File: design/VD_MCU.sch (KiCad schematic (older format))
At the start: 2 parts

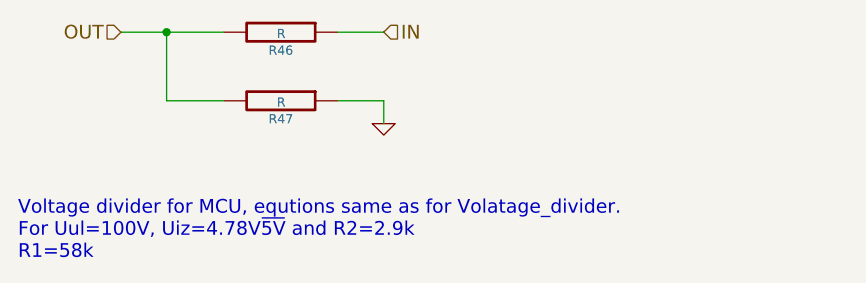
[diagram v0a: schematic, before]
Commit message: Fix some ERC error, add decoupling cap to Vref+ and make some small changes to lib
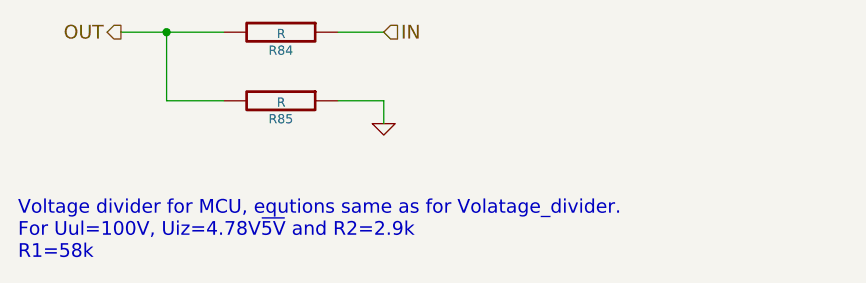
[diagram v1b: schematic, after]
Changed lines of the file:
@@
 AR Path="/54B735D5/54E0E40F/54E0BCE1" Ref="R82"  Part="1"
 AR Path="/54B735D5/54E0E5A3/54E0BCE1" Ref="R84"  Part="1"
-F 0 "R46" V 5530 3200 40  0000 C CNN
+F 0 "R84" V 5530 3200 40  0000 C CNN
 F 1 "R" V 5457 3201 40  0000 C CNN
 F 2 "" V 5380 3200 30  0000 C CNN
@@
 AR Path="/54B735D5/54E0E40F/54E0BD13" Ref="R83"  Part="1"
 AR Path="/54B735D5/54E0E5A3/54E0BD13" Ref="R85"  Part="1"
-F 0 "R47" V 5530 3500 40  0000 C CNN
+F 0 "R85" V 5530 3500 40  0000 C CNN
 F 1 "R" V 5457 3501 40  0000 C CNN
 F 2 "" V 5380 3500 30  0000 C CNN
@@
 P 5900 3600
 AR Path="/504F83BE/54E0B9B4/54E0BD65" Ref="#PWR?"  Part="1"
-AR Path="/504F83BE/54E0E125/54E0BD65" Ref="#PWR68"  Part="1"
-AR Path="/504F83BE/54E0E40F/54E0BD65" Ref="#PWR69"  Part="1"
-AR Path="/504F83BE/54E0E5A3/54E0BD65" Ref="#PWR70"  Part="1"
-AR Path="/54B735D5/54E0E125/54E0BD65" Ref="#PWR101"  Part="1"
-AR Path="/54B735D5/54E0E40F/54E0BD65" Ref="#PWR102"  Part="1"
-AR Path="/54B735D5/54E0E5A3/54E0BD65" Ref="#PWR103"  Part="1"
-F 0 "#PWR68" H 5900 3600 30  0001 C CNN
+AR Path="/504F83BE/54E0E125/54E0BD65" Ref="#PWR070"  Part="1"
+AR Path="/504F83BE/54E0E40F/54E0BD65" Ref="#PWR071"  Part="1"
+AR Path="/504F83BE/54E0E5A3/54E0BD65" Ref="#PWR072"  Part="1"
+AR Path="/54B735D5/54E0E125/54E0BD65" Ref="#PWR0106"  Part="1"
+AR Path="/54B735D5/54E0E40F/54E0BD65" Ref="#PWR0107"  Part="1"
+AR Path="/54B735D5/54E0E5A3/54E0BD65" Ref="#PWR0108"  Part="1"
+F 0 "#PWR0108" H 5900 3600 30  0001 C CNN
 F 1 "GND" H 5900 3530 30  0001 C CNN
 F 2 "" H 5900 3600 60  0000 C CNN
@@
 Text HLabel 5900 3200 2    60   Input ~ 0
 IN
-Text HLabel 4750 3200 0    60   Input ~ 0
+Text HLabel 4750 3200 0    60   Output ~ 0
 OUT
 Text Notes 4300 4200 0    60   ~ 0
